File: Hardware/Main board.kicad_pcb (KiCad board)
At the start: 4 copper layers, 60.7 x 40 mm, 163 parts, among them IC1 LTC4413EDD#PBF, J1 ST1W008S4TR2000, J2 USB_C_Receptacle_USB2.0, J3 XT30PW-M, J4 USB_C_Receptacle_USB2.0, J5 7788, J6 7788, Q2 BSZ025N04LS, Q3 BSZ025N04LS, Q4 BSZ025N04LS, Q6 SSM3K15AMFV,L3F, Q8 DMP3099L, U1 ESP32-S3, U10 TPS55288QRPMRQ1, U11 DPS368, U12 TCMT1109, U2 SN65HVD230, U3 LM66200DRLR, U4 MAX77827AEFD+T, U5 SC4215ASTRT, U7 BU27006MUC-ZTR, U8 INA219AxDCN, Y1 R940000171

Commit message: Extra tweaks - current sense etc
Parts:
- TP5: moved to F.Cu
- moved TP5 18.1 mm to (144.0, 103.2), turned to -90 degrees
- moved C8 0.20 mm to (121.0, 95.5)
- moved R3 0.18 mm to (122.1, 95.5)
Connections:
- U1 pad 21: /GPIO15 -> unconnected-(U1-GPIO15/ADC2_CH4/XTAL_32K_P-Pad21)
- U1 pad 22: /GPIO16 -> unconnected-(U1-GPIO16/ADC2_CH5/XTAL_32K_N-Pad22)
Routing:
- net /Voltage Regulation/ISN_2: track 10.6 -> 17.6 mm
- net /PyroPWR: track 0.00 -> 6.72 mm
- net RBUS_uC_V: track 33.8 -> 27.8 mm, vias 1 -> 0
- net +3V3: track 41.7 -> 43.9 mm

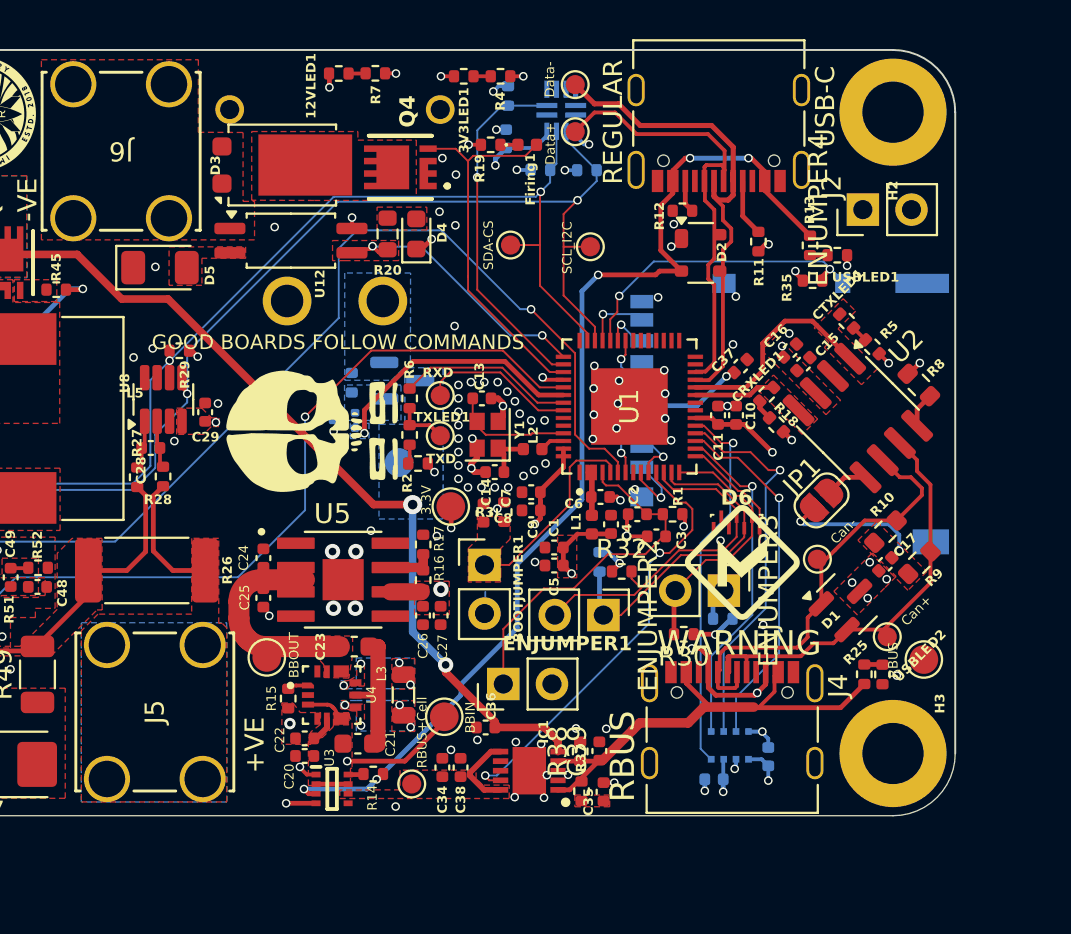
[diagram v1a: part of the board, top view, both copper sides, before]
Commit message: Silkscreen for gpio breakout
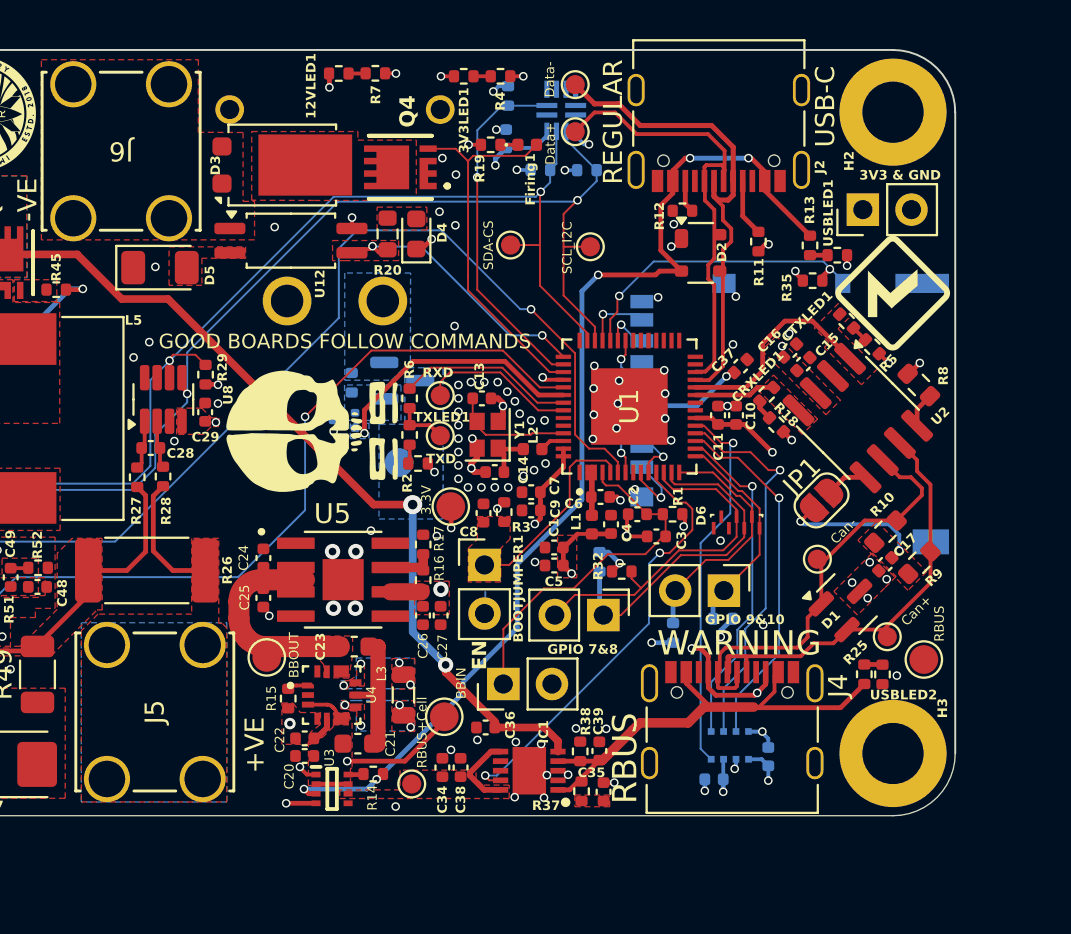
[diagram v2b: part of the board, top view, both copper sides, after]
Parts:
- 3V3 & GND: renamed from ENJUMPER4
- GPIO 7&8: renamed from ENJUMPER2
- GPIO 9&10: renamed from ENJUMPER3
- R30: moved to B.Cu
- moved G*** 16.1 mm to (142.4, 84.0)
- moved R29 1.85 mm to (106.5, 88.3), turned to 90 degrees
- moved R30 0.56 mm to (130.9, 101.8), turned to 90 degrees
- renumbered ENJUMPER1 to EN
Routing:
- net /SDA: track 67.4 -> 69.1 mm
- net +3V3: vias 26 -> 27

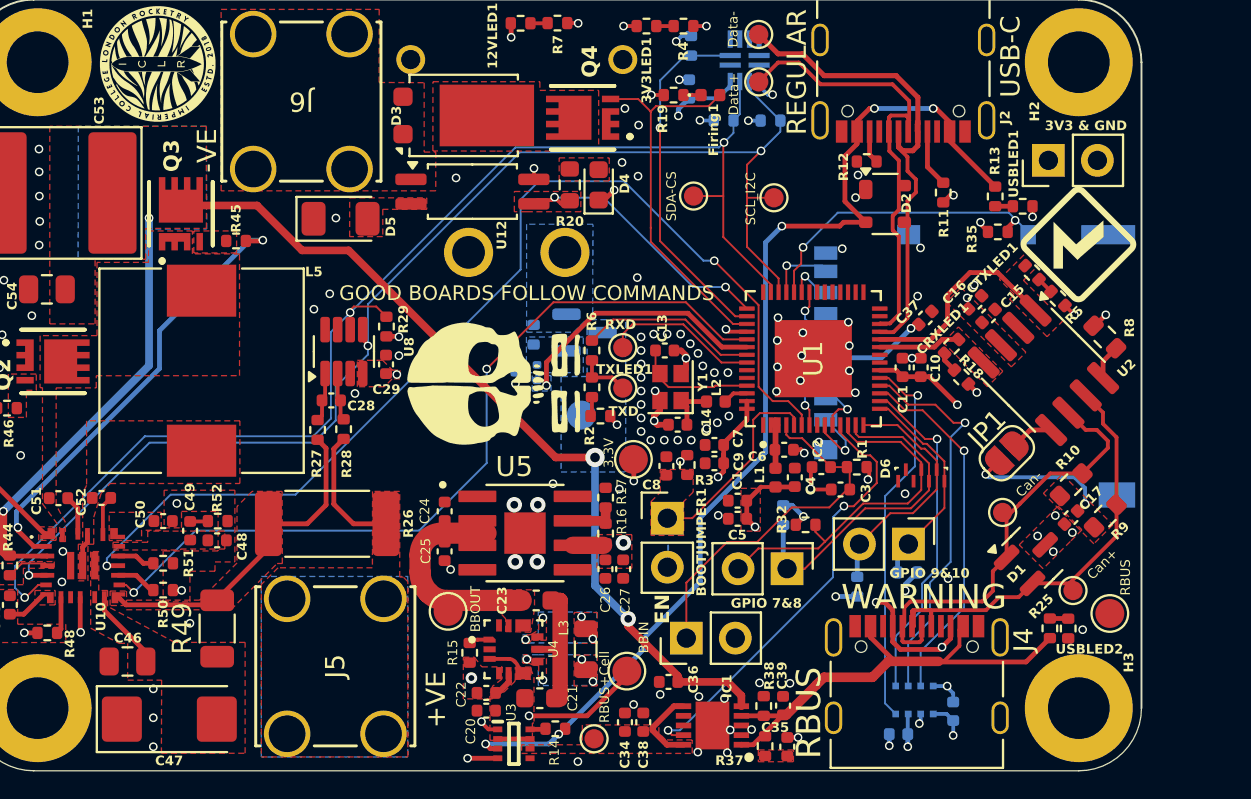
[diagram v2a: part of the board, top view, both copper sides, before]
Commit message: Changed mosfet + added top plane for Cell_+ and fixed silkscreen
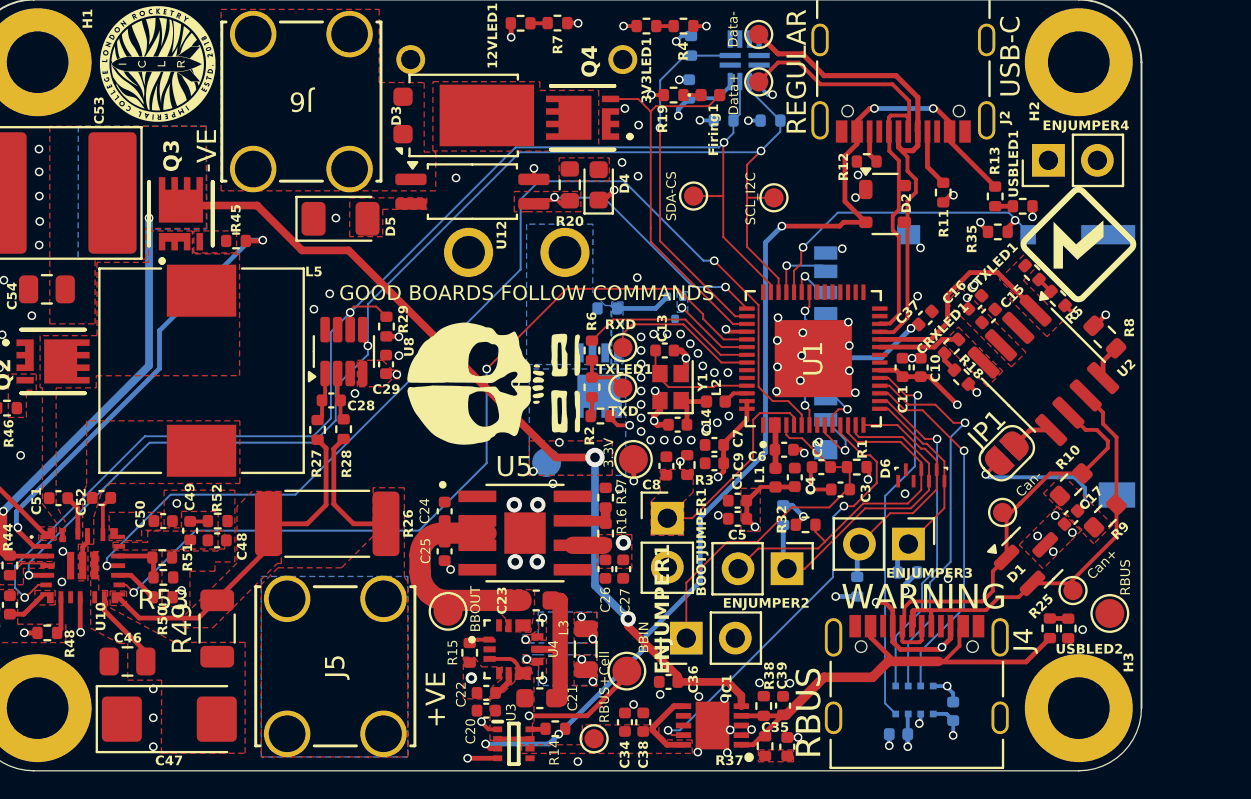
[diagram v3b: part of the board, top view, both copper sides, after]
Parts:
- removed Q8: DMP3099L, Package_TO_SOT_SMD:SOT-23
- added Q1: SISS23DN-T1-GE3, iclr:SQS850ENT1_GE3, B.Cu at (117.5, 91.1)
- added R53: 165k, Resistor_SMD:R_0402_1005Metric, F.Cu at (94.9, 101.3)
- ENJUMPER2: renamed from GPIO 7&8
- ENJUMPER3: renamed from GPIO 9&10
- ENJUMPER4: renamed from 3V3 & GND
- R51: value 31.6k -> 165k
- moved Q6 8.43 mm to (121.5, 87.3), turned to -90 degrees
- moved R36 4.06 mm to (118.0, 87.4), turned to 180 degrees
- moved TP14 3.05 mm to (114.8, 95.3)
- moved G*** 2.51 mm to (111.9, 82.7)
- moved R50 0.37 mm to (94.9, 102.3)
- moved R51 0.30 mm to (94.9, 100.3)
- renumbered EN to ENJUMPER1
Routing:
- net /Cell-switch: track 13.4 -> 4.21 mm
- net Net-(Q1-G): track 0.00 -> 2.85 mm
- net Net-(U10-ILIM): track 1.98 -> 2.86 mm
- net /INT: track 42.6 -> 43.3 mm
- net +3V3: track 43.9 -> 44.6 mm
- net /Voltage Regulation/ISN_2: track 17.6 -> 18.1 mm
- net GND: track 47.2 -> 46.7 mm, vias 123 -> 122
- net Cell_+: vias 4 -> 6

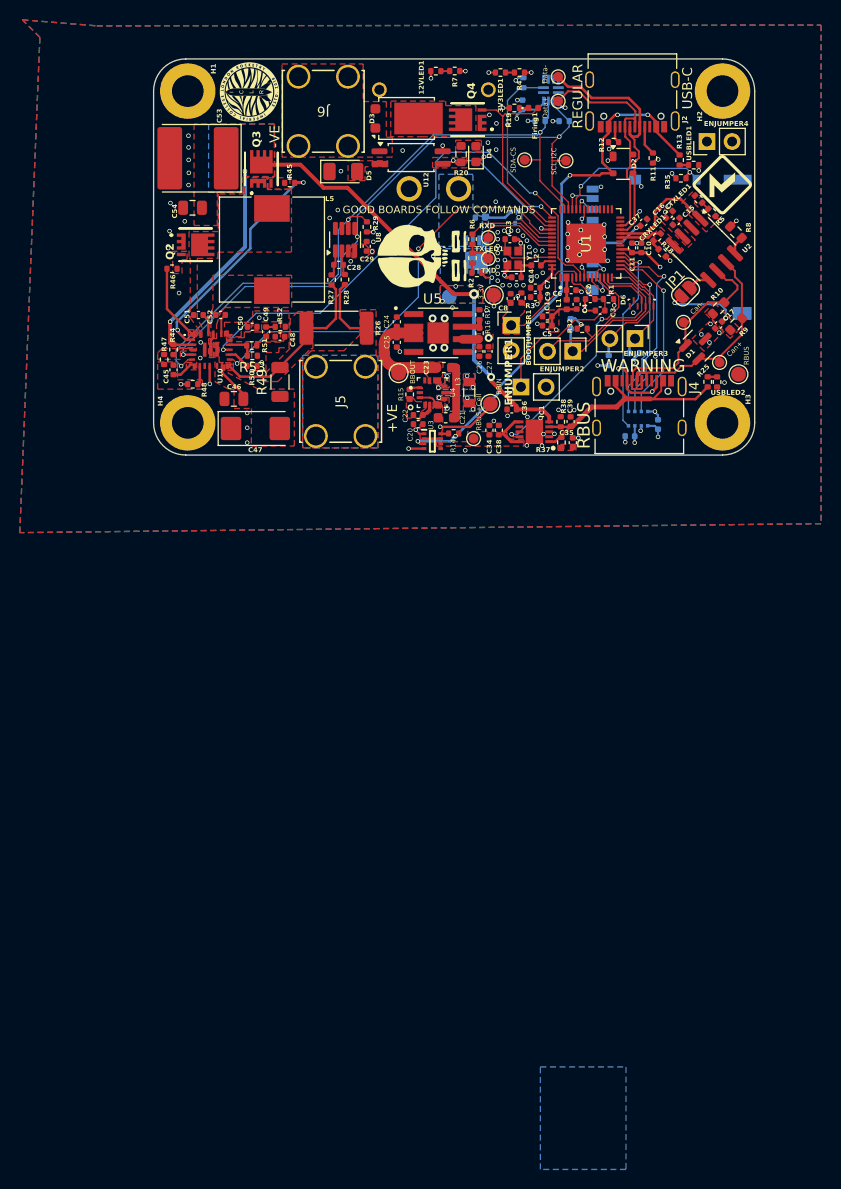
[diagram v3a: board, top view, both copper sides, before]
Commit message: Changed buck boost inductor + changed planes and vias
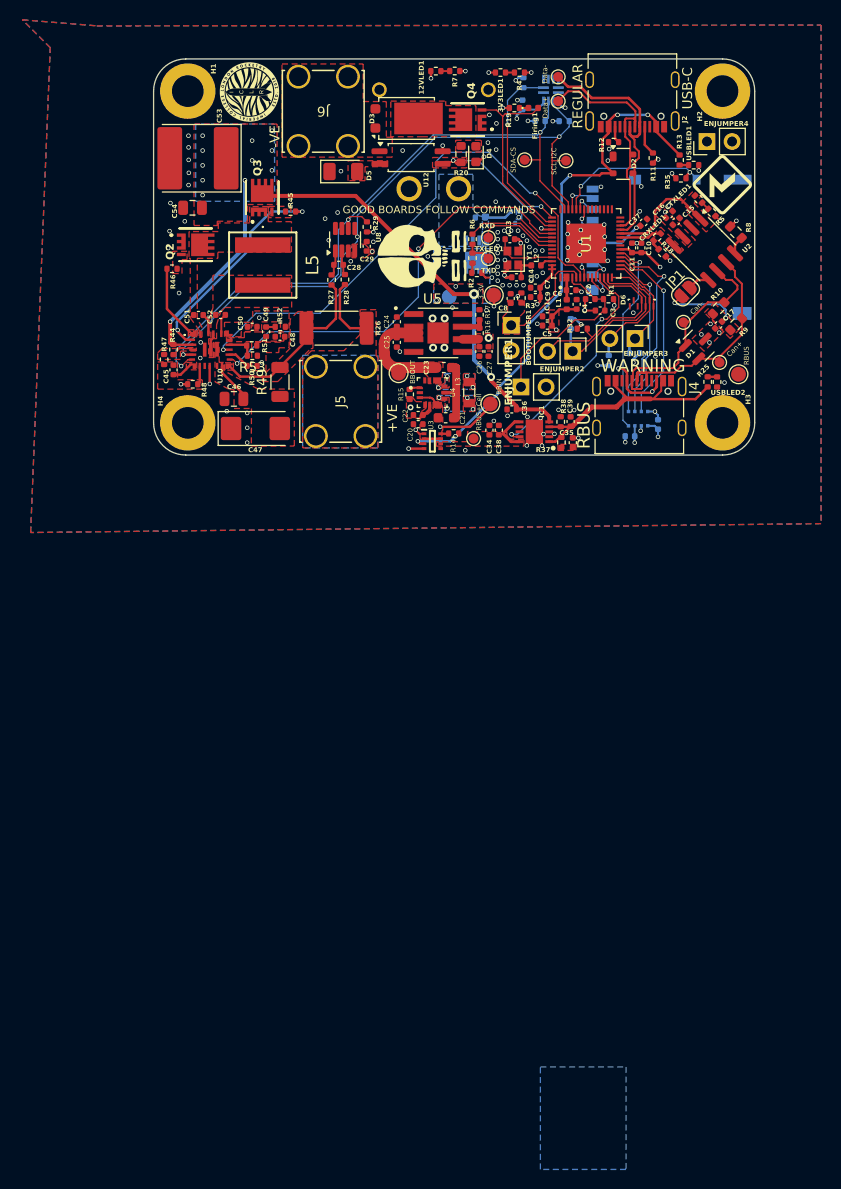
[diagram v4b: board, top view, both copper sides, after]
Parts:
- L5: value 4.7uH -> PA5432472NLT; footprint Inductor_SMD:L_10.4x10.4_H4.8 -> iclr:PA5432472NLT
- moved R45 2.89 mm to (98.8, 86.8)
- moved Q3 2.89 mm to (95.9, 85.3)
- moved L5 1.82 mm to (96.0, 92.2), turned to 180 degrees
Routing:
- net Cell_+: track 67.3 -> 65.1 mm, vias 6 -> 16
- net Net-(U10-DR1H): track 23.5 -> 21.7 mm
- net GND: vias 122 -> 124
